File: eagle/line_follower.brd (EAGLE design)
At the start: 100 x 80 mm, 44 parts, among them IC1 A4950, IC2 A4950, IC3 7805DT, IC4 LM317LD, J1 XT-60NO_LABEL, J2 22-27-2031-03, SW1 12MM_BUTTON, U1 TEENSY_3.1_BASIC, U2 MPU6050_BREAKOUT, X1 1.5MM_PAD, X2 1.5MM_PAD, X3 1.5MM_PAD, X4 1.5MM_PAD

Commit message: Fixes before sending the board for fab.
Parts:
- removed U$1: LINE_FOLLOWER_HEATSINK, untitled:LINE_FOLLOWER_HEATSINK
- removed U1: TEENSY_3.1_BASIC, Teensy_3_Series_Board_v1.0:TEENSY_3.1_BASIC
- removed U2: MPU6050_BREAKOUT, untitled:MPU6050_BREAKOUT
- added M1B, M2A: 1.5MM_PAD, untitled:1.5MM_PAD
- C2, C3: value 100nF -> 100uF 16V; device rcl:C0805 -> rcl:UD-6,3X5,8_NICHICON
- C4, C6: value 100uF 16V -> 100nF; device rcl:UD-6,3X5,8_NICHICON -> rcl:C0805
- Q1, Q2, Q3, Q4: device SparkFun-DiscreteSemi:PT17-21C-L41-TR8 -> untitled:PHOTOTRANSISTOR1206
- R6, R7: value 0R15 -> 1R 1% 0.125W; device rcl:R2512 -> rcl:R0805
- R8: value 470 -> 4k7
- R9: value 470 -> 1k5
- X1: value 1.5MM_PAD -> TEENSY_3.1_BASIC; device untitled:1.5MM_PAD -> Teensy_3_Series_Board_v1.0:TEENSY_3.1_BASIC
- X2: value 1.5MM_PAD -> MPU6050_BREAKOUT; device untitled:1.5MM_PAD -> untitled:MPU6050_BREAKOUT
- moved X2 58.2 mm to (22.9, 39.4), turned to 180 degrees
- moved X1 47.3 mm to (41.9, 31.8), turned to 180 degrees
- moved C2 36.4 mm to (62.2, 27.9), turned to 0 degrees
- moved C3 32.4 mm to (62.2, 50.8)
- moved C4 27.9 mm to (54.6, 63.5), turned to 270 degrees
- moved C6 24.2 mm to (86.4, 29.2)
- moved C1 13.1 mm to (68.6, 39.4)
- moved IC4 3.81 mm to (29.2, 66.7)
- moved R5 3.81 mm to (22.9, 66.7)
- moved R8 2.54 mm to (45.7, 12.7)
- moved R9 2.54 mm to (38.1, 12.7)
- turned J2 to 180 degrees
- turned Q1 to 180 degrees
- turned Q2 to 180 degrees
- turned Q3 to 180 degrees
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- renumbered C5 to C7, X3 to M1A, X4 to M2B
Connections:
- net +3V3: now also Q1.C, Q2.C, Q3.C, Q4.C, X1.3.3V, X1.3.3V1; no longer IC1.4, IC2.4, U1.3.3V, U1.3.3V1
- net +5V: now also C4.1, IC1.4, IC2.4, X1.VIN, X2.P$1; no longer C2.1, Q1.C, Q2.C, Q3.C, Q4.C, U1.VIN, U2.P$1
- net BUTTON: now also X1.12; no longer U1.12
- net GND: now also C2.-, C3.-, C4.2, C6.2, X1.AGND, X1.GND, X1.GND1, X2.P$2; no longer C2.2, C3.2, C4.-, C6.-, U$1.P$1, U1.AGND, U1.GND, U1.GND1, U2.P$2
- net I_SENSE0: now also X1.21/A7; no longer U1.21/A7
- net I_SENSE1: now also X1.20/A6; no longer U1.20/A6
- net LINE0: now also X1.17/A3; no longer U1.17/A3
- net LINE1: now also X1.16/A2; no longer U1.16/A2
- net LINE2: now also X1.15/A1; no longer U1.15/A1
- net LINE3: now also X1.14/A0; no longer U1.14/A0
- net LINE_LED0: now also X1.7; no longer U1.7
- net LINE_LED1: now also X1.8; no longer U1.8
- net LINE_LED2: now also X1.9; no longer U1.9
- net LINE_LED3: now also X1.10; no longer U1.10
- net LINE_LED4: now also X1.11; no longer U1.11
- net MOTOR0A: now also X1.3; no longer U1.3
- net MOTOR0B: now also X1.4; no longer U1.4
- net MOTOR1A: now also X1.5; no longer U1.5
- net MOTOR1B: now also X1.6; no longer U1.6
- net N$3: now also M2A.P$1; no longer X2.P$1
- net N$4: now also M1B.P$1; no longer X1.P$1
- net N$5: now also C3.+; no longer C1.+
- net RANGE: now also X1.23/A9; no longer U1.23/A9
- net SCL: now also X1.19/A5, X2.P$3; no longer U1.19/A5, U2.P$3
- net SDA: now also X1.18/A4, X2.P$4; no longer U1.18/A4, U2.P$4
- net U_SENSE: now also X1.22/A8; no longer U1.22/A8
- net VBAT: now also X1.VBAT; no longer U1.VBAT
- net VCC: now also C1.+, C2.+, C6.1; no longer C3.1, C4.+, C6.+
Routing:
- net GND: track 375.3 -> 471.8 mm
- net VCC: track 129.7 -> 118.6 mm, vias 6 -> 5
- net RANGE: track 17.0 -> 24.2 mm
- net +3V3: track 96.9 -> 101.1 mm, vias 1 -> 0
- net +5V: track 194.3 -> 197.3 mm, vias 1 -> 2
- net U_SENSE: track 27.1 -> 24.6 mm
- net LINE3: track 34.7 -> 32.7 mm
- net LINE1: track 32.7 -> 30.7 mm
- net LINE0: track 42.7 -> 40.7 mm
- net I_SENSE1: track 74.7 -> 76.5 mm
- net N$11: track 98.2 -> 96.5 mm
- net LINE2: track 30.6 -> 29.1 mm
- net LINE_LED1: track 50.5 -> 51.6 mm
- net I_SENSE0: track 65.0 -> 66.0 mm
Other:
- board text added: "3S LiPo"
- board text added: "Line follower https://github.com/bluecube Apr 2016"

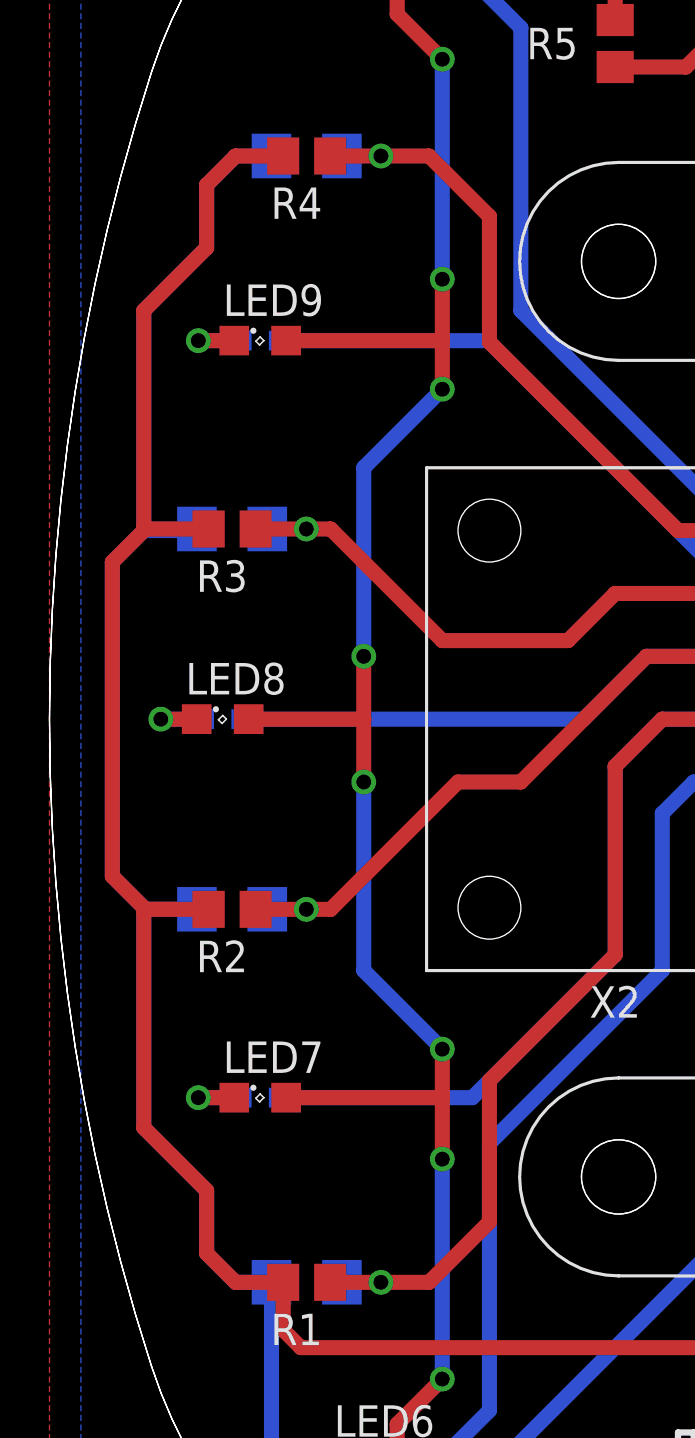
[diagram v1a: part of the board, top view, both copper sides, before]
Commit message: Added missing connections to the board.
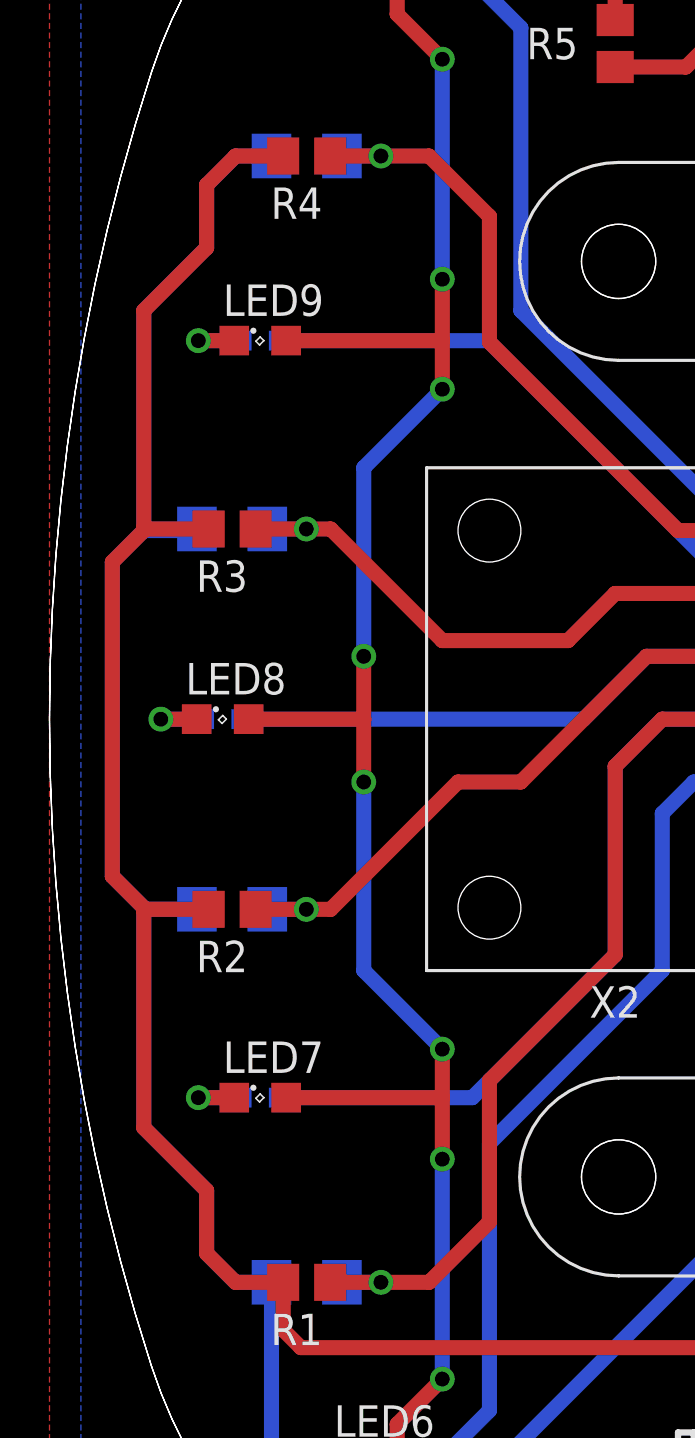
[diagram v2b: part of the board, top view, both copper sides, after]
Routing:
- net LINE3: track 32.7 -> 34.3 mm
- net LINE0: track 40.7 -> 42.3 mm
- net LINE2: track 29.1 -> 30.7 mm
- net LINE1: track 30.7 -> 32.3 mm
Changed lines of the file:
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@@
 <grid distance="0.05" unitdist="inch" unit="mm" style="lines" multiple="1" display="no" altdistance="0.635" altunitdist="mm" altunit="mm"/>
 <layers>
-<layer number="1" name="Top" color="4" fill="1" visible="yes" active="yes"/>
+<layer number="1" name="Top" color="4" fill="1" visible="no" active="yes"/>
 <layer number="16" name="Bottom" color="1" fill="1" visible="yes" active="yes"/>
 <layer number="17" name="Pads" color="2" fill="1" visible="yes" active="yes"/>
@@
 <wire x1="19.05" y1="36.83" x2="24.13" y2="41.91" width="0.6096" layer="1"/>
 <wire x1="24.13" y1="41.91" x2="27.94" y2="41.91" width="0.6096" layer="1"/>
-<wire x1="8.8016" y1="31.68406875" x2="8.3296" y2="31.68406875" width="0" layer="19" extent="1-16"/>
+<wire x1="8.8016" y1="31.68406875" x2="10.3796" y2="31.68406875" width="0.6096" layer="16"/>
 </signal>
 <signal name="LINE2">
@@
 <wire x1="22.86" y1="44.45" x2="20.955" y2="42.545" width="0.6096" layer="1"/>
 <wire x1="20.955" y1="42.545" x2="15.875" y2="42.545" width="0.6096" layer="1"/>
-<wire x1="8.8016" y1="47.05593125" x2="8.3296" y2="47.05593125" width="0" layer="19" extent="1-16"/>
+<wire x1="8.8016" y1="47.05593125" x2="10.3796" y2="47.05593125" width="0.6096" layer="16"/>
 </signal>
 <signal name="LINE3">
@@
 <wire x1="15.340709375" y1="62.129290625" x2="17.78" y2="59.69" width="0.6096" layer="1"/>
 <contactref element="Q4" pad="E"/>
-<wire x1="11.81626875" y1="62.129290625" x2="11.34426875" y2="62.129290625" width="0" layer="19" extent="1-16"/>
+<wire x1="11.81626875" y1="62.129290625" x2="13.39426875" y2="62.129290625" width="0.6096" layer="16"/>
 </signal>
 <signal name="LINE0">
@@
 <wire x1="24.765" y1="39.37" x2="27.94" y2="39.37" width="0.6096" layer="1"/>
 <contactref element="Q1" pad="E"/>
-<wire x1="11.81626875" y1="16.610709375" x2="11.34426875" y2="16.610709375" width="0" layer="19" extent="1-16"/>
+<wire x1="11.81626875" y1="16.610709375" x2="13.39426875" y2="16.610709375" width="0.6096" layer="16"/>
 </signal>
 <signal name="VCC">

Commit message: Fixed values of line sensor divider resistors.
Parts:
- R1, R2, R3, R4: value 470 -> 10k
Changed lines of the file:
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@@
 <?xml version="1.0" encoding="utf-8"?>
 <!DOCTYPE eagle SYSTEM "eagle.dtd">
-<eagle version="7.4.0">
+<eagle version="7.7.0">
 <drawing>
 <settings>
@@
 <grid distance="0.05" unitdist="inch" unit="mm" style="lines" multiple="1" display="no" altdistance="0.635" altunitdist="mm" altunit="mm"/>
 <layers>
-<layer number="1" name="Top" color="4" fill="1" visible="no" active="yes"/>
+<layer number="1" name="Top" color="4" fill="1" visible="yes" active="yes"/>
 <layer number="16" name="Bottom" color="1" fill="1" visible="yes" active="yes"/>
 <layer number="17" name="Pads" color="2" fill="1" visible="yes" active="yes"/>
@@
 <attribute name="VALUE" x="11.73" y="71.275" size="1.27" layer="28" rot="MR180"/>
 </element>
-<element name="R1" library="rcl" package="R0805" value="470" x="10.39426875" y="16.610709375" smashed="yes" rot="R180">
+<element name="R1" library="rcl" package="R0805" value="10k" x="10.39426875" y="16.610709375" smashed="yes" rot="R180">
 <attribute name="NAME" x="11.02926875" y="15.340709375" size="1.27" layer="25" rot="R180"/>
 </element>
-<element name="R2" library="rcl" package="R0805" value="470" x="7.3796" y="31.68406875" smashed="yes" rot="R180">
+<element name="R2" library="rcl" package="R0805" value="10k" x="7.3796" y="31.68406875" smashed="yes" rot="R180">
 <attribute name="NAME" x="8.0146" y="30.41406875" size="1.27" layer="25" rot="R180"/>
 </element>
-<element name="R3" library="rcl" package="R0805" value="470" x="7.3796" y="47.05593125" smashed="yes" rot="R180">
+<element name="R3" library="rcl" package="R0805" value="10k" x="7.3796" y="47.05593125" smashed="yes" rot="R180">
 <attribute name="NAME" x="8.0146" y="45.78593125" size="1.27" layer="25" rot="R180"/>
 </element>
-<element name="R4" library="rcl" package="R0805" value="470" x="10.39426875" y="62.129290625" smashed="yes" rot="R180">
+<element name="R4" library="rcl" package="R0805" value="10k" x="10.39426875" y="62.129290625" smashed="yes" rot="R180">
 <attribute name="NAME" x="11.02926875" y="60.859290625" size="1.27" layer="25" rot="R180"/>
 </element>

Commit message: Schematic for V2 mostly complete, time to work on the board.
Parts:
- removed IC4: LM317LD, linear:SO08
- removed LED10, LED7, LED8, LED9: (no value), led:SML0805
- removed M1A, M1B, M2A, M2B: 1.5MM_PAD, untitled:1.5MM_PAD
- removed R6, R7: 1R 1% 0.125W, rcl:R0805
- removed R8: 4k7, rcl:R0805
- added C10, C11, C12, C8, C9: 100n, rcl:C0805
- added C5: 100nF, rcl:C0805
- added J3, J4: 22-27-2061-06, con-molex:6410-06
- added Q5: ALS-PT19-315C/L177/TR8, untitled:PHOTOTRANSISTOR-1.7MM
- added R10: 1k5, rcl:R0805
- C1, C2, C3: value 100uF 16V -> 100uF 25V
- IC3: value 7805DT -> MC78M05 (??)
- J1: value XT-60NO_LABEL -> 2S - 4S LiPo
- LED1, LED2, LED3, LED4, LED5: value (none) -> APT2012EC; device led:CHIPLED_0603 -> led:CHIP-LED0805
- LED6: value (none) -> APT2012EC; device led:SML0805 -> led:CHIP-LED0805
- Q1, Q2, Q3, Q4: value (none) -> ALS-PT19-315C/L177/TR8; device untitled:PHOTOTRANSISTOR1206 -> untitled:PHOTOTRANSISTOR-1.7MM
- R1, R2, R3, R4: value 10k -> 5k6
- R5: value 68 -> 5k6
- R9: value 1k5 -> 4k7
- X1: value TEENSY_3.1_BASIC -> ESP32DEVKITV1; device Teensy_3_Series_Board_v1.0:TEENSY_3.1_BASIC -> ESP32-DEVKITV1:ESP32-DEVKITV1
- moved Q4 326.4 mm to (2.54, -264.2), flipped to the top, turned to 0 degrees
- moved Q3 304.9 mm to (2.54, -257.8), flipped to the top, turned to 0 degrees
- moved Q2 283.2 mm to (2.54, -251.5), flipped to the top, turned to 0 degrees
- moved Q1 261.8 mm to (2.54, -245.1), flipped to the top, turned to 0 degrees
- moved R4 256.6 mm to (2.54, -194.3), turned to 0 degrees
- moved R5 249.1 mm to (2.54, -181.6), turned to 0 degrees
- moved R3 247.8 mm to (2.54, -200.7), turned to 0 degrees
- moved R2 238.7 mm to (2.54, -207.0), turned to 0 degrees
- moved R1 230.1 mm to (2.54, -213.4), turned to 0 degrees
- moved X1 186.9 mm to (33.0, -154.9), turned to 0 degrees
- moved C4 150.3 mm to (2.54, -77.5), flipped to the top, turned to 0 degrees
- moved C7 32.4 mm to (54.6, 63.5), turned to 270 degrees
- moved LED6 30.3 mm to (2.54, -19.1)
- moved C6 27.9 mm to (86.4, 57.1)
- moved C3 26.2 mm to (85.1, 63.5)
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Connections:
- removed net I_SENSE0: IC1.7, R6.1, X1.21/A7
- removed net I_SENSE1: IC2.7, R7.1, X1.20/A6
- removed net LINE0: Q1.E, R1.1, X1.17/A3
- removed net LINE1: Q2.E, R2.1, X1.16/A2
- removed net LINE2: Q3.E, R3.1, X1.15/A1
- removed net LINE3: Q4.E, R4.1, X1.14/A0
- removed net LINE_LED3: LED4.C, X1.10
- removed net LINE_LED4: LED5.C, X1.11
- removed net N$10: LED4.A, LED9.C
- removed net N$11: IC4.4, LED10.A, LED6.A, LED7.A, LED8.A, LED9.A, R5.2
- removed net N$12: LED10.C, LED5.A
- removed net N$14: IC4.2, IC4.3, IC4.6, IC4.7, R5.1
- removed net N$5: C3.+, D1.C, IC3.1
- removed net N$8: LED3.A, LED8.C
- removed net U_SENSE: R8.2, R9.1, X1.22/A8
- removed net VBAT: X1.VBAT
- new net BAT_SENSE: R10.1, R9.2, X1.26
- new net ENCODER0A: J3.3, X1.8
- new net ENCODER0B: J3.4, X1.7
- new net ENCODER1A: J4.4, X1.4
- new net ENCODER1B: J4.3, X1.3
- new net LINE_SENSOR0: C8.2, Q1.E, R1.2, X1.21
- new net LINE_SENSOR1: C9.2, Q2.E, R2.2, X1.28
- new net LINE_SENSOR2: C10.2, Q3.E, R3.2, X1.22
- new net LINE_SENSOR3: C11.2, Q4.E, R4.2, X1.27
- new net LINE_SENSOR4: C12.2, Q5.E, R5.2, X1.19
- new net MPU6050_INT: X1.13, X2.P$8
- net +3V3: now also IC1.4, IC2.4, J3.2, J4.2, Q5.C, X1.1; no longer X1.3.3V, X1.3.3V1
- net +5V: now also C1.+, D1.C, X1.30; no longer C4.1, IC1.4, IC2.4, IC3.2, IC4.1, X1.VIN
- net GND: now also C10.1, C11.1, C12.1, C5.2, C8.1, C9.1, IC1.7, IC2.7, J3.5, J4.5, R1.1, R10.2, R2.1, R3.1, R4.1, R5.1, X1.2, X1.28; no longer R1.2, R2.2, R3.2, R4.2, R6.2, R7.2, R9.2, X1.AGND, X1.GND, X1.GND1
- net LINE_LED0: now also LED2.A, LED5.C, LED6.A, X1.24; no longer X1.7
- net LINE_LED1: now also LED1.A, LED3.C, LED4.A, X1.24; no longer X1.8
- net LINE_LED2: now also LED3.A, LED4.C, LED5.A, LED6.C, X1.23; no longer LED3.C, X1.9
- net MOTOR0A: now also IC1.3, X1.10; no longer IC1.2, X1.3
- net MOTOR0B: now also IC1.2, X1.9; no longer IC1.3, X1.4
- net MOTOR1A: now also X1.6; no longer X1.5
- net MOTOR1B: now also X1.5; no longer X1.6
- net N$1: now also J3.1; no longer M1A.P$1
- net N$2: now also IC2.6, J4.1; no longer IC2.8, M2B.P$1
- net N$3: now also IC2.8, J4.6; no longer IC2.6, M2A.P$1
- net N$4: now also J3.6; no longer M1B.P$1
- net N$6: now also C7.1, D1.A, IC3.2; no longer LED1.A, LED6.C
- net N$7: now also C4.1, IC3.1; no longer LED2.A, LED7.C
- net RANGE: now also X1.20; no longer X1.23/A9
- net SCL: now also X1.14; no longer X1.19/A5
- net SDA: now also X1.11; no longer X1.18/A4
- net VCC: now also C3.+, C5.1, R9.1; no longer C1.+, C7.1, D1.A, R8.1
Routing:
- net GND: track 471.8 -> 274.9 mm, vias 49 -> 30
- net +5V: track 197.3 -> 10.7 mm, vias 2 -> 0
- net VCC: track 118.6 -> 0.00 mm, vias 5 -> 0
- net N$11: track 96.5 -> 0.00 mm, vias 8 -> 0
- net I_SENSE1: track 76.5 -> 0.00 mm, vias 1 -> 0
- net I_SENSE0: track 66.0 -> 0.00 mm, vias 1 -> 0
- net LINE_LED0: track 57.7 -> 0.00 mm
- net LINE_LED4: track 53.0 -> 0.00 mm
- net LINE_LED1: track 51.6 -> 0.00 mm
- net LINE_LED3: track 45.0 -> 0.00 mm
- net LINE_LED2: track 43.4 -> 0.00 mm
- net LINE0: track 42.3 -> 0.00 mm, vias 1 -> 0
- net LINE3: track 34.3 -> 0.00 mm, vias 1 -> 0
- net +3V3: track 101.1 -> 134.8 mm, vias 0 -> 2
- net LINE1: track 32.3 -> 0.00 mm, vias 1 -> 0
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- removed copper zone on layer 1, net GND
- removed copper zone on layer 16, net GND

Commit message: Updated gitignore
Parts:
- R10: value 1k5 -> 15k
- R9: value 4k7 -> 82k
- moved Q1 312.7 mm to (15.2, 67.3), flipped to the bottom, turned to 180 degrees
- moved Q2 311.2 mm to (10.2, 59.7), flipped to the bottom, turned to 180 degrees
- moved Q3 306.1 mm to (8.89, 48.3), flipped to the bottom, turned to 180 degrees
- moved Q4 296.0 mm to (7.62, 31.8), flipped to the bottom, turned to 180 degrees
- moved Q5 288.4 mm to (10.2, 17.8), flipped to the bottom, turned to 180 degrees
- moved C8 272.7 mm to (36.8, 31.8), turned to 180 degrees
- moved C9 268.9 mm to (36.8, 34.3), turned to 180 degrees
- moved C10 267.6 mm to (36.8, 39.4), turned to 180 degrees
- moved C11 266.4 mm to (36.8, 44.5), turned to 180 degrees
- moved R1 257.2 mm to (21.6, 43.2)
- moved R2 246.2 mm to (36.8, 36.8), turned to 180 degrees
- moved R3 245.0 mm to (36.8, 41.9), turned to 180 degrees
- moved R4 243.7 mm to (36.8, 47.0), turned to 180 degrees
- moved C12 240.0 mm to (36.8, 49.5), turned to 180 degrees
- moved R5 236.2 mm to (36.8, 52.1), turned to 180 degrees
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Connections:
- removed net MPU6050_INT: X1.13, X2.P$8
- net BUTTON: now also X1.8; no longer X1.12
- net ENCODER0A: no longer X1.8
- net ENCODER0B: no longer X1.7
- net ENCODER1A: now also X1.28; no longer X1.4
- net ENCODER1B: now also X1.6; no longer X1.3
- net GND: now also X1.29; no longer X1.28
- net LINE_LED0: now also X1.25; no longer X1.24
- net LINE_SENSOR1: now also X1.3; no longer X1.28
- net LINE_SENSOR3: now also X1.5; no longer X1.27
- net MOTOR1A: no longer X1.6
- net MOTOR1B: now also X1.27; no longer X1.5
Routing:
- net +3V3: track 134.8 -> 0.00 mm, vias 2 -> 0
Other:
- board text added: "Line follower v2.0 https://github.com/bluecube/line_follower Apr 2020"
- board text removed: "Line follower https://github.com/bluecube Apr 2016"

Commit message: Rough layout of the new board
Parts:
- moved J2 31.9 mm to (61.0, 5.08), turned to 90 degrees
- moved X2 27.3 mm to (35.6, 63.5), turned to 90 degrees
- moved R1 25.7 mm to (35.6, 21.6), turned to 180 degrees
- moved SW1 25.0 mm to (63.5, 72.4)
- moved X1 10.9 mm to (35.6, 30.5)
- moved R4 10.2 mm to (35.6, 36.8)
- moved R5 10.2 mm to (35.6, 41.9)
- moved R2 10.2 mm to (35.6, 26.7)
- moved R3 10.2 mm to (35.6, 31.8)
- moved Q3 9.58 mm to (5.33, 39.4)
- moved LED3 9.13 mm to (5.63, 32.4)
- moved LED4 8.07 mm to (5.63, 46.4)
- moved C8 7.73 mm to (38.1, 24.1)
- moved Q2 7.35 mm to (6.52, 53.3)
- moved Q4 6.41 mm to (6.52, 25.4)
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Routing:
- net GND: track 274.9 -> 4.71 mm, vias 30 -> 4
- net MOTOR1A: track 47.4 -> 0.00 mm, vias 1 -> 0
- net MOTOR1B: track 44.1 -> 0.00 mm, vias 1 -> 0
- net MOTOR0B: track 43.6 -> 0.00 mm, vias 1 -> 0
- net MOTOR0A: track 42.6 -> 0.00 mm, vias 1 -> 0
- net RANGE: track 23.0 -> 0.00 mm
- net BAT_SENSE: track 19.5 -> 0.00 mm
- net BUTTON: track 11.2 -> 0.00 mm
- net N$7: track 10.8 -> 0.00 mm
- net +5V: track 10.7 -> 0.00 mm
- net SDA: track 4.86 -> 0.00 mm
- net SCL: track 4.86 -> 0.00 mm
- net N$6: track 1.88 -> 0.00 mm
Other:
- outline, holes or cut-outs redrawn
